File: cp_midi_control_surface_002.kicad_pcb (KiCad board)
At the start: 2 copper layers, 185 parts, among them J1 Conn_01x08_Male, J10 Conn_01x08_Female, J11 Conn_01x08_Female, J12 Conn_01x08_Female, J13 Conn_01x08_Female, J14 Conn_01x08_Female, J15 Conn_01x08_Female, J16 Conn_01x08_Female, J17 Conn_01x08_Female, J18 Conn_01x01_Male, J19 Conn_01x01_Male, J2 Conn_01x08_Male, J20 Conn_01x01_Male, J21 Conn_01x01_Male, J22 Conn_01x01_Male, J23 Conn_01x01_Male, J3 Conn_01x08_Male, J4 Conn_01x01_Male, J5 Conn_01x01_Male, J6 Conn_01x01_Male, J7 Conn_01x01_Male, J8 Conn_01x08_Male, J9 Conn_01x08_Male, P1 Digital, P10 CONN_01X01, P11 CONN_01X01, P12 CONN_01X01, P13 CONN_01X01, P2 Power, P3 Analogue, P4 Analogue, P5 PWM, P6 PWM, P7 Communication, P8 CONN_01X01, P9 CONN_01X01, SW1 SW_SPST_4_PIN, SW10 SW_SPST_4_PIN, SW11 SW_SPST_4_PIN, SW12 SW_SPST_4_PIN, SW13 SW_SPST_4_PIN, SW14 SW_SPST_4_PIN, SW15 SW_SPST_4_PIN, SW16 SW_SPST_4_PIN, SW17 SW_SPST_4_PIN, SW18 SW_SPST_4_PIN, SW19 SW_SPST_4_PIN, SW2 SW_SPST_4_PIN, SW20 SW_SPST_4_PIN, SW21 SW_SPST_4_PIN, SW22 SW_SPST_4_PIN, SW23 SW_SPST_4_PIN, SW24 SW_SPST_4_PIN, SW25 SW_SPST_4_PIN, SW26 SW_SPST_4_PIN, SW27 SW_SPST_4_PIN, SW28 SW_SPST_4_PIN, SW29 SW_SPST_4_PIN, SW3 SW_SPST_4_PIN, SW30 SW_SPST_4_PIN, SW31 SW_SPST_4_PIN, SW32 SW_SPST_4_PIN, SW33 SW_SPST_4_PIN, SW34 SW_SPST_4_PIN, SW35 SW_SPST_4_PIN, SW36 SW_SPST_4_PIN, SW37 SW_SPST_4_PIN, SW38 SW_SPST_4_PIN, SW39 SW_SPST_4_PIN, SW4 SW_SPST_4_PIN, SW40 SW_SPST_4_PIN, SW41 SW_SPST_4_PIN, SW42 SW_SPST_4_PIN, SW43 SW_SPST_4_PIN, SW44 SW_SPST_4_PIN, SW45 SW_SPST_4_PIN, SW46 SW_SPST_4_PIN, SW47 SW_SPST_4_PIN, SW48 SW_SPST_4_PIN, SW49 SW_SPST_4_PIN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

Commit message: First of changes due to different software
Moving and analogue inputs, correcting for placement of multiplexer pads.
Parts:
- removed P4: Analogue, Connector_PinHeader_2.54mm:PinHeader_1x08_P2.54mm_Vertical
- P7: footprint Connector_PinHeader_2.54mm:PinHeader_1x08_P2.54mm_Vertical -> Connector_PinHeader_2.54mm:PinHeader_1x04_P2.54mm_Vertical
- moved H1 199.0 mm to (764.4, 381.0)
- moved H10 199.0 mm to (761.1, 395.1)
- moved H11 199.0 mm to (759.4, 401.3)
- moved H13 199.0 mm to (765.8, 395.1)
- moved H14 199.0 mm to (754.7, 401.3)
- moved H2 199.0 mm to (759.7, 385.7)
- moved H21 199.0 mm to (761.1, 390.4)
- moved H22 199.0 mm to (746.9, 391.9)
- moved H24 199.0 mm to (746.9, 396.6)
- moved H3 199.0 mm to (759.7, 381.0)
- moved H5 199.0 mm to (764.4, 385.7)
- moved H7 199.0 mm to (773.9, 381.0)
- moved H8 199.0 mm to (773.9, 385.7)
- moved H9 199.0 mm to (765.8, 390.4)
- moved J10 199.0 mm to (737.4, 400.7)
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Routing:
- net /A2: track 342.2 -> 0.00 mm
- net /A3: track 316.7 -> 0.00 mm
- net /A4: track 291.1 -> 0.00 mm
- net /A5: track 265.6 -> 0.00 mm
- net /A6: track 240.1 -> 0.00 mm
- net /A7: track 214.5 -> 0.00 mm
- net /A1: track 367.8 -> 167.6 mm
- net /A8: track 186.5 -> 0.00 mm
- net +5V: track 1386.4 -> 1350.2 mm

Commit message: Sub boards completed
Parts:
- added J24: Conn_01x04_Male, Connector_PinHeader_2.54mm:PinHeader_1x04_P2.54mm_Vertical, F.Cu at (180.0, 239.2)
- added U6: CD74HC4067M, Package_SO:SOIC-24W_7.5x15.4mm_P1.27mm, B.Cu at (421.4, 273.6)
- H1, H10, H11, H12, H13, H14, H15, H16, H17, H18, H19, H2, H20, H21, H22, H23, H24, H25, H26, H3, H4, H5, H6, H7, H8, H9: footprint cunabulapress-footprints:Mounting_Hole_3.2mm_M3 -> cunabulapress-footprints:Mounting_Hole_M3_with_Target
- J11: moved to B.Cu
- J3: value Conn_01x08_Male -> Conn_01x04_Male; footprint Connector_PinHeader_2.54mm:PinHeader_1x08_P2.54mm_Vertical -> Connector_PinHeader_2.54mm:PinHeader_1x04_P2.54mm_Vertical
- moved H1 726.8 mm to (74.2, 153.0)
- moved H3 709.4 mm to (74.2, 198.0)
- moved H2 651.9 mm to (150.8, 153.0)
- moved J11 649.0 mm to (116.7, 259.5)
- moved H4 645.7 mm to (150.8, 198.2)
- moved H5 643.7 mm to (164.2, 153.0)
- moved H7 636.5 mm to (164.2, 198.0)
- moved H6 577.4 mm to (240.8, 153.0)
- moved H8 565.2 mm to (240.8, 198.0)
- moved H9 557.9 mm to (264.0, 146.7)
- moved H11 534.5 mm to (264.0, 200.7)
- moved J6 518.9 mm to (70.2, 249.2)
- moved J4 510.6 mm to (70.2, 236.8)
- moved J16 476.9 mm to (206.7, 199.3)
- moved H10 474.3 mm to (357.0, 146.7)
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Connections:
- net /A10 renamed /Lower Pots/LOWER_POTS
- net /A8 renamed Net-(RV8-Pad2)
- J10 pad 1: Mult_1 -> S0
- J10 pad 2: Mult_2 -> S1
- J10 pad 3: Mult_3 -> S3
- J10 pad 4: Mult_4 -> S2
- J10 pad 5: /A9 -> /A0
- J11 pad 1: Mult_1 -> S0
- J11 pad 2: Mult_2 -> S1
- J11 pad 3: Mult_3 -> S3
- J11 pad 4: Mult_4 -> S2
- J11 pad 5: /52 -> /A1
- J12 pad 1: Mult_1 -> S0
- J12 pad 2: Mult_2 -> S1
- J12 pad 3: Mult_3 -> S3
- J12 pad 4: Mult_4 -> S2
- J12 pad 5: /50 -> /A2
- J13 pad 1: Mult_1 -> S0
- J13 pad 2: Mult_2 -> S1
- J13 pad 3: Mult_3 -> S3
- J13 pad 4: Mult_4 -> S2
- J13 pad 5: /48 -> /A3
- J3 pad 1: /46 -> Net-(J3-Pad1)
- J3 pad 2: /44 -> Net-(J3-Pad2)
- J3 pad 3: /42 -> Net-(J3-Pad3)
- J3 pad 4: /40 -> Net-(J3-Pad4)
- P1 pad 10: /36 -> /37
- P1 pad 11: /34 -> /35
- P1 pad 12: /32 -> /33
- P1 pad 14: /28 -> S2
- P1 pad 15: /26 -> S3
- P1 pad 16: Net-(P1-Pad16) -> S1
- P1 pad 17: Net-(P1-Pad17) -> S0
- P1 pad 2: /52 -> /53
- P1 pad 3: /50 -> /51
- P1 pad 4: /48 -> /49
- P1 pad 5: /46 -> /47
- P1 pad 6: /44 -> /45
- P1 pad 7: /42 -> /43
- P1 pad 8: /40 -> /41
- P1 pad 9: /38 -> /39
- P3 pad 7: /A6 -> Net-(P3-Pad7)
- P3 pad 8: /A7 -> Net-(P3-Pad8)
- RV1 pad 2: /A1 -> Net-(RV1-Pad2)
- RV2 pad 2: /A2 -> Net-(RV2-Pad2)
- RV3 pad 2: /A3 -> Net-(RV3-Pad2)
- RV4 pad 2: /A4 -> Net-(RV4-Pad2)
- RV5 pad 2: /A5 -> Net-(RV5-Pad2)
- RV6 pad 2: /A6 -> Net-(RV6-Pad2)
- RV7 pad 2: /A7 -> Net-(RV7-Pad2)
- RVM1 pad 2: /A0 -> Net-(RVM1-Pad2)
- SW1 pad 3: GND -> Net-(SW1-Pad3)
- SW1 pad 4: Net-(SW1-Pad4) -> GND
- SW33 pad 1: Net-(SW33-Pad1) -> Net-(J3-Pad1)
- SW33 pad 2: /46 -> Net-(SW33-Pad2)
- SW34 pad 1: Net-(SW34-Pad1) -> Net-(J3-Pad2)
- SW34 pad 2: /44 -> Net-(SW34-Pad2)
- SW35 pad 1: Net-(SW35-Pad1) -> Net-(J3-Pad3)
- SW35 pad 2: /42 -> Net-(SW35-Pad2)
- SW36 pad 1: Net-(SW36-Pad1) -> Net-(J3-Pad4)
- SW36 pad 2: /40 -> Net-(SW36-Pad2)
- SW37 pad 1: /38 -> Net-(J24-Pad1)
- SW38 pad 1: /36 -> Net-(J24-Pad2)
- SW39 pad 1: /34 -> Net-(J24-Pad3)
- SW40 pad 1: /32 -> Net-(J24-Pad4)
- SW_F1 pad 12: /A0 -> Net-(RVM1-Pad2)
- SW_F1 pad 14: /A7 -> Net-(RV7-Pad2)
- SW_F1 pad 15: /A6 -> Net-(RV6-Pad2)
- SW_F1 pad 16: /A5 -> Net-(RV5-Pad2)
- SW_F1 pad 17: /A4 -> Net-(RV4-Pad2)
- SW_F1 pad 18: /A3 -> Net-(RV3-Pad2)
- SW_F1 pad 19: /A2 -> Net-(RV2-Pad2)
- SW_F1 pad 20: /A1 -> Net-(RV1-Pad2)
- SW_M1 pad A: /28 -> /37
- SW_M1 pad B: /26 -> /35
- U1 pad 13: Net-(J15-Pad4) -> Net-(J15-Pad3)
- U1 pad 14: Net-(J15-Pad3) -> Net-(J15-Pad4)
- U2 pad 13: Net-(J16-Pad4) -> Net-(J16-Pad3)
- U2 pad 14: Net-(J16-Pad3) -> Net-(J16-Pad4)
- U3 pad 13: Net-(J14-Pad4) -> Net-(J14-Pad3)
- U3 pad 14: Net-(J14-Pad3) -> Net-(J14-Pad4)
- U4 pad 13: Net-(J17-Pad4) -> Net-(J17-Pad3)
- U4 pad 14: Net-(J17-Pad3) -> Net-(J17-Pad4)
- U5 pad 10: Mult_1 -> S0
- U5 pad 11: Mult_2 -> S1
- U5 pad 13: Mult_4 -> S3
- U5 pad 14: Mult_3 -> S2
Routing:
- net +5V: track 1350.2 -> 1074.5 mm, vias 0 -> 3
- net /A1: track 167.6 -> 0.00 mm
- net Net-(J14-Pad5): track 185.2 -> 45.9 mm, vias 0 -> 1
- net Net-(J17-Pad5): track 138.8 -> 41.4 mm, vias 0 -> 1
- net Net-(J15-Pad5): track 135.6 -> 41.3 mm, vias 0 -> 1
- net Net-(J16-Pad5): track 134.7 -> 41.3 mm, vias 0 -> 1
- net Net-(J14-Pad1): track 85.2 -> 26.8 mm
- net Net-(J14-Pad2): track 80.2 -> 22.3 mm
- net Net-(J24-Pad2): track 0.00 -> 57.3 mm
- net Net-(J3-Pad3): track 0.00 -> 57.3 mm
- net Net-(J14-Pad3): track 79.5 -> 23.9 mm
- net Net-(J14-Pad4): track 74.2 -> 23.7 mm
- net Net-(J3-Pad2): track 0.00 -> 33.3 mm
- net Net-(J24-Pad3): track 0.00 -> 33.3 mm
- net Net-(J15-Pad1): track 54.7 -> 22.2 mm
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
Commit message: Tidy schematic / renumber components / complete daughter boards
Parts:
- removed the J5 at (244.8, 236.8)
- removed the J6 at (70.2, 249.2)
- removed the J8 at (654.5, 169.8)
- removed the P1 at (374.5, 266.8)
- removed the P5 at (452.3, 310.0)
- removed the U1 at (112.5, 175.5)
- added J13: ~, Connector_PinHeader_2.54mm:PinHeader_1x01_P2.54mm_Vertical, B.Cu at (262.8, 89.2)
- added J14: ~, Connector_PinSocket_2.54mm:PinSocket_1x01_P2.54mm_Vertical, F.Cu at (70.2, 236.8)
- added J15: ~, Connector_PinHeader_2.54mm:PinHeader_1x01_P2.54mm_Vertical, B.Cu at (437.2, 89.2)
- added J25: ~, Connector_PinHeader_2.54mm:PinHeader_1x08_P2.54mm_Vertical, B.Cu at (379.9, 112.8)
- added J26: ~, Connector_PinSocket_2.54mm:PinSocket_1x08_P2.54mm_Vertical, F.Cu at (270.0, 236.0)
- added J27: ~, Connector_PinHeader_2.54mm:PinHeader_1x08_P2.54mm_Vertical, B.Cu at (443.1, 112.8)
- added J28: ~, Connector_PinSocket_2.54mm:PinSocket_1x08_P2.54mm_Vertical, F.Cu at (333.2, 236.0)
- added P2: Analogue, Connector_PinHeader_2.54mm:PinHeader_1x08_P2.54mm_Vertical, B.Cu at (420.3, 262.7)
- added P6: PWM, Connector_PinHeader_2.54mm:PinHeader_1x10_P2.54mm_Vertical, B.Cu at (452.3, 311.0)
- added REF**: Clearance_Hole_M3, cunabulapress-footprints:Clearance_Hole_M3, F.Cu at (350.0, 95.5)
- added U6: CD74HC4067M, Package_SO:SOIC-24W_7.5x15.4mm_P1.27mm, B.Cu at (310.0, 281.5)
- D1, D10, D11, D12, D13, D14, D15, D16, D2, D3, D4, D5, D6, D7, D8, D9: value ~ -> LED
- H1, H10, H11, H12, H13, H14, H15, H16, H17, H18, H19, H2, H20, H21, H22, H23, H24, H25, H26, H3, H4, H5, H6, H7, H8, H9: value MountingHole -> ~
- J1, J2: value Conn_01x08_Male -> ~; footprint Connector_PinHeader_2.54mm:PinHeader_1x08_P2.54mm_Vertical -> cunabulapress-footprints:Connector_TE_Connectivity_Micro-MaTch_8_Position_Female; moved to B.Cu
- J10, J12: value Conn_01x08_Female -> ~; footprint cunabulapress-footprints:Connector_TE_Connectivity_Micro-MaTch_8_Position_Female -> Connector_PinSocket_2.54mm:PinSocket_1x04_P2.54mm_Vertical; moved to F.Cu
- J11: value Conn_01x08_Female -> ~; footprint cunabulapress-footprints:Connector_TE_Connectivity_Micro-MaTch_8_Position_Female -> Connector_PinHeader_2.54mm:PinHeader_1x04_P2.54mm_Vertical
- J16: value Conn_01x08_Female -> ~; footprint cunabulapress-footprints:Connector_TE_Connectivity_Micro-MaTch_8_Position_Female -> Connector_PinSocket_2.54mm:PinSocket_1x01_P2.54mm_Vertical; moved to F.Cu
- J17: value Conn_01x08_Female -> ~; footprint cunabulapress-footprints:Connector_TE_Connectivity_Micro-MaTch_8_Position_Female -> Connector_PinHeader_2.54mm:PinHeader_1x01_P2.54mm_Vertical
- J18, J20: value Conn_01x01_Male -> ~; footprint cunabulapress-footprints:Arduino_1pin_EDIT -> Connector_PinSocket_2.54mm:PinSocket_1x01_P2.54mm_Vertical
- J19: value Conn_01x01_Male -> ~; footprint cunabulapress-footprints:Arduino_1pin_EDIT -> Connector_PinHeader_2.54mm:PinHeader_1x01_P2.54mm_Vertical; moved to B.Cu
- J21, J23: value Conn_01x01_Male -> ~; footprint cunabulapress-footprints:Arduino_1pin_EDIT -> Connector_PinHeader_2.54mm:PinHeader_1x08_P2.54mm_Vertical; moved to B.Cu
- J22: value Conn_01x01_Male -> ~; footprint cunabulapress-footprints:Arduino_1pin_EDIT -> Connector_PinSocket_2.54mm:PinSocket_1x08_P2.54mm_Vertical
- J24: value Conn_01x04_Male -> ~; footprint Connector_PinHeader_2.54mm:PinHeader_1x04_P2.54mm_Vertical -> Connector_PinSocket_2.54mm:PinSocket_1x08_P2.54mm_Vertical
- J3: value Conn_01x04_Male -> ~; footprint Connector_PinHeader_2.54mm:PinHeader_1x04_P2.54mm_Vertical -> cunabulapress-footprints:Connector_TE_Connectivity_Micro-MaTch_8_Position_Female; moved to B.Cu
- J4, J7: value Conn_01x01_Male -> ~; footprint Connector_PinHeader_2.54mm:PinHeader_1x01_P2.54mm_Vertical -> cunabulapress-footprints:Connector_TE_Connectivity_Micro-MaTch_8_Position_Female; moved to B.Cu
- J5: renamed from J13; value Conn_01x08_Female -> ~
- J6: renamed from J15; value Conn_01x08_Female -> ~
- J8: renamed from J14; value Conn_01x08_Female -> ~
- J9: value Conn_01x08_Male -> ~; footprint Connector_PinHeader_2.54mm:PinHeader_1x08_P2.54mm_Vertical -> Connector_PinHeader_2.54mm:PinHeader_1x04_P2.54mm_Vertical; moved to B.Cu
- P10, P11, P12, P13, P8, P9: value CONN_01X01 -> Guide
- P3: value Analogue -> Digital; footprint Connector_PinHeader_2.54mm:PinHeader_1x08_P2.54mm_Vertical -> Connector_PinHeader_2.54mm:PinHeader_1x18_P2.54mm_Vertical
- RN1: value R_Network09 -> 2.2K (Bussed)
- RN2, RN3: value R_Network08 -> 680Ω (Bussed)
- RV1, RV2, RV3, RV4, RV5, RV6, RV7, RV8, RVM1: value 10k -> PTA4543
- RVCF1: value R_POT -> PTA4543
- SW1, SW10, SW11, SW12, SW13, SW14, SW15, SW16, SW17, SW18, SW19, SW2, SW20, SW21, SW22, SW23, SW24, SW25, SW26, SW27, SW28, SW29, SW3, SW30, SW31, SW32, SW33, SW34, SW35, SW36, SW37, SW38, SW39, SW4, SW40, SW41, SW42, SW43, SW44, SW45, SW46, SW47, SW48, SW49, SW5, SW50, SW51, SW52, SW53, SW54, SW55, SW56, SW6, SW7, SW8, SW9: value SW_SPST_4_PIN -> B3F-5050
- SW_M1: value Mode Switch -> EC12E
- moved SW_F1 671.7 mm to (-67.8, 227.2), turned to 90 degrees
- moved RN1 602.1 mm to (-24.2, 219.8)
- moved J1 545.9 mm to (116.7, 199.3)
- moved J2 541.6 mm to (116.7, 259.5)
- moved J18 455.7 mm to (70.2, 249.2)
- moved H23 427.7 mm to (157.5, 326.2)
- moved H18 416.2 mm to (157.2, 243.0)
- moved RN2 364.9 mm to (267.4, 232.2)
- moved J9 339.8 mm to (327.5, 91.8), turned to 180 degrees
- moved H19 325.2 mm to (252.0, 243.0)
- moved U1 324.1 mm to (112.5, 175.5), turned to 180 degrees
- moved H24 319.9 mm to (251.3, 326.0)
- moved J11 305.9 mm to (372.5, 91.8), turned to 180 degrees
- moved RN3 302.2 mm to (330.7, 232.2)
- moved J20 295.1 mm to (244.8, 249.2)
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- renumbered P2 to P1, P7 to P4, P6 to P5, U6 to U1, U3 to U2, U5 to U3, U2 to U5
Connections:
- D1 pad 2: /17 -> Net-(D1-Pad2)
- D10 pad 2: /7 -> Net-(D10-Pad2)
- D11 pad 2: /8 -> Net-(D11-Pad2)
- D12 pad 2: /9 -> Net-(D12-Pad2)
- D13 pad 2: /10 -> Net-(D13-Pad2)
- D14 pad 2: /11 -> Net-(D14-Pad2)
- D15 pad 2: /12 -> Net-(D15-Pad2)
- D16 pad 2: /13 -> Net-(D16-Pad2)
- D2 pad 2: /16 -> Net-(D2-Pad2)
- D3 pad 2: /15 -> Net-(D3-Pad2)
- D4 pad 2: /14 -> Net-(D4-Pad2)
- D5 pad 2: /2 -> Net-(D5-Pad2)
- D6 pad 2: /3 -> Net-(D6-Pad2)
- D7 pad 2: /4 -> Net-(D7-Pad2)
- D8 pad 2: /5 -> Net-(D8-Pad2)
- D9 pad 2: /6 -> Net-(D9-Pad2)
- J1 pad 1: /17 -> Net-(J1-Pad1)
- J1 pad 2: /16 -> Net-(J1-Pad2)
- J1 pad 3: /15 -> Net-(J1-Pad3)
- J1 pad 4: /14 -> Net-(J1-Pad4)
- J1 pad 5: /2 -> Net-(J1-Pad5)
- J1 pad 6: /3 -> +5V
- J1 pad 7: /4 -> GND
- J1 pad 8: /5 -> Net-(J1-Pad8)
- J10 pad 1: S0 -> /53
- J10 pad 2: S1 -> /51
- J10 pad 3: S3 -> /49
- J10 pad 4: S2 -> /47
- J11 pad 1: S0 -> Net-(J11-Pad1)
- J11 pad 2: S1 -> Net-(J11-Pad2)
- J11 pad 3: S3 -> Net-(J11-Pad3)
- J11 pad 4: S2 -> Net-(J11-Pad4)
- J12 pad 1: S0 -> /45
- J12 pad 2: S1 -> /43
- J12 pad 3: S3 -> /41
- J12 pad 4: S2 -> /39
- J16 pad 1: Net-(J16-Pad1) -> GND
- J17 pad 1: Net-(J17-Pad1) -> GND
- J2 pad 1: /6 -> S0
- J2 pad 2: /7 -> S1
- J2 pad 3: /8 -> S3
- J2 pad 4: /9 -> S2
- J2 pad 5: /10 -> /A0
- J2 pad 6: /11 -> +5V
- J2 pad 7: /12 -> GND
- J2 pad 8: /13 -> Net-(J2-Pad8)
- J24 pad 1: Net-(J24-Pad1) -> /6
- J24 pad 2: Net-(J24-Pad2) -> /7
- J24 pad 3: Net-(J24-Pad3) -> /8
- J24 pad 4: Net-(J24-Pad4) -> /9
- J4 pad 1: GND -> S0
- J5 pad 1: S0 -> Net-(J5-Pad1)
- J5 pad 2: S1 -> Net-(J5-Pad2)
- J5 pad 3: S3 -> Net-(J5-Pad3)
- J5 pad 4: S2 -> Net-(J5-Pad4)
- J5 pad 5: /A3 -> Net-(J5-Pad5)
- J6 pad 1: Net-(J15-Pad1) -> S0
- J6 pad 2: Net-(J15-Pad2) -> S1
- J6 pad 3: Net-(J15-Pad3) -> S3
- J6 pad 4: Net-(J15-Pad4) -> S2
- J6 pad 5: Net-(J15-Pad5) -> /A2
- J7 pad 1: GND -> Net-(J7-Pad1)
- J8 pad 1: Net-(J14-Pad1) -> S0
- J8 pad 2: Net-(J14-Pad2) -> S1
- J8 pad 3: Net-(J14-Pad3) -> S3
- J8 pad 4: Net-(J14-Pad4) -> S2
- J8 pad 5: Net-(J14-Pad5) -> /A3
- J9 pad 1: Net-(D9-Pad1) -> Net-(J9-Pad1)
- J9 pad 2: Net-(D10-Pad1) -> Net-(J9-Pad2)
- J9 pad 3: Net-(D11-Pad1) -> Net-(J9-Pad3)
- J9 pad 4: Net-(D12-Pad1) -> Net-(J9-Pad4)
- P3 pad 1: /A0 -> GND
- P3 pad 2: /A1 -> /53
- P3 pad 3: /A2 -> /51
- P3 pad 4: /A3 -> /49
- P3 pad 5: /A4 -> /47
- P3 pad 6: /A5 -> /45
- P3 pad 7: Net-(P3-Pad7) -> /43
- P3 pad 8: Net-(P3-Pad8) -> /41
- RN2 pad 2: Net-(D1-Pad1) -> Net-(J26-Pad1)
- RN2 pad 3: Net-(D2-Pad1) -> Net-(J26-Pad2)
- RN2 pad 4: Net-(D3-Pad1) -> Net-(J26-Pad3)
- RN2 pad 5: Net-(D4-Pad1) -> Net-(J26-Pad4)
- RN2 pad 6: Net-(D5-Pad1) -> Net-(J26-Pad5)
- RN2 pad 7: Net-(D6-Pad1) -> Net-(J26-Pad6)
- RN2 pad 8: Net-(D7-Pad1) -> Net-(J26-Pad7)
- RN2 pad 9: Net-(D8-Pad1) -> Net-(J26-Pad8)
- RN3 pad 2: Net-(D9-Pad1) -> Net-(J28-Pad1)
- RN3 pad 3: Net-(D10-Pad1) -> Net-(J28-Pad2)
- RN3 pad 4: Net-(D11-Pad1) -> Net-(J28-Pad3)
- RN3 pad 5: Net-(D12-Pad1) -> Net-(J28-Pad4)
- RN3 pad 6: Net-(D13-Pad1) -> Net-(J28-Pad5)
- RN3 pad 7: Net-(D14-Pad1) -> Net-(J28-Pad6)
- RN3 pad 8: Net-(D15-Pad1) -> Net-(J28-Pad7)
- RN3 pad 9: Net-(D16-Pad1) -> Net-(J28-Pad8)
- SW33 pad 1: Net-(J3-Pad1) -> Net-(J9-Pad1)
- SW34 pad 1: Net-(J3-Pad2) -> Net-(J9-Pad2)
- SW35 pad 1: Net-(J3-Pad3) -> Net-(J9-Pad3)
- SW36 pad 1: Net-(J3-Pad4) -> Net-(J9-Pad4)
- SW37 pad 1: Net-(J24-Pad1) -> Net-(J11-Pad1)
- SW38 pad 1: Net-(J24-Pad2) -> Net-(J11-Pad2)
- SW39 pad 1: Net-(J24-Pad3) -> Net-(J11-Pad3)
- SW40 pad 1: Net-(J24-Pad4) -> Net-(J11-Pad4)
- SW_F1 pad 1: Net-(RN1-Pad10) -> Net-(RV1-Pad2)
- SW_F1 pad 12: Net-(RVM1-Pad2) -> Net-(RN1-Pad2)
- SW_F1 pad 13: Net-(RV8-Pad2) -> Net-(RN1-Pad3)
- SW_F1 pad 14: Net-(RV7-Pad2) -> Net-(RN1-Pad4)
- SW_F1 pad 15: Net-(RV6-Pad2) -> Net-(RN1-Pad5)
- SW_F1 pad 16: Net-(RV5-Pad2) -> Net-(RN1-Pad6)
- SW_F1 pad 17: Net-(RV4-Pad2) -> Net-(RN1-Pad7)
- SW_F1 pad 18: Net-(RV3-Pad2) -> Net-(RN1-Pad8)
- SW_F1 pad 19: Net-(RV2-Pad2) -> Net-(RN1-Pad9)
- SW_F1 pad 2: Net-(RN1-Pad9) -> Net-(RV2-Pad2)
- SW_F1 pad 20: Net-(RV1-Pad2) -> Net-(RN1-Pad10)
- SW_F1 pad 3: Net-(RN1-Pad8) -> Net-(RV3-Pad2)
- SW_F1 pad 4: Net-(RN1-Pad7) -> Net-(RV4-Pad2)
- SW_F1 pad 5: Net-(RN1-Pad6) -> Net-(RV5-Pad2)
- SW_F1 pad 6: Net-(RN1-Pad5) -> Net-(RV6-Pad2)
- SW_F1 pad 7: Net-(RN1-Pad4) -> Net-(RV7-Pad2)
- SW_F1 pad 8: Net-(RN1-Pad3) -> Net-(RV8-Pad2)
- SW_F1 pad 9: Net-(RN1-Pad2) -> Net-(RVM1-Pad2)
- U1 pad 1: /A5 -> Net-(J1-Pad5)
- U1 pad 10: S0 -> Net-(J1-Pad1)
- U1 pad 11: S1 -> Net-(J1-Pad2)
- U1 pad 13: S3 -> Net-(J1-Pad3)
- U1 pad 14: S2 -> Net-(J1-Pad4)
- U1 pad 16: Net-(U6-Pad16) -> Net-(SW16-Pad1)
- U1 pad 17: Net-(U6-Pad17) -> Net-(SW15-Pad1)
- U1 pad 18: Net-(U6-Pad18) -> Net-(SW14-Pad1)
- U1 pad 19: Net-(U6-Pad19) -> Net-(SW13-Pad1)
- U1 pad 2: Net-(RV8-Pad2) -> Net-(SW8-Pad1)
- U1 pad 20: Net-(U6-Pad20) -> Net-(SW12-Pad2)
- U1 pad 21: Net-(U6-Pad21) -> Net-(SW11-Pad2)
- U1 pad 22: Net-(U6-Pad22) -> Net-(SW10-Pad2)
- U1 pad 23: Net-(RVM1-Pad2) -> Net-(SW9-Pad2)
- U1 pad 3: Net-(RV7-Pad2) -> Net-(SW7-Pad1)
- U1 pad 4: Net-(RV6-Pad2) -> Net-(SW6-Pad1)
- U1 pad 5: Net-(RV5-Pad2) -> Net-(SW5-Pad1)
- U1 pad 6: Net-(RV4-Pad2) -> Net-(SW4-Pad2)
- U1 pad 7: Net-(RV3-Pad2) -> Net-(SW3-Pad2)
- U1 pad 8: Net-(RV2-Pad2) -> Net-(SW2-Pad2)
- U1 pad 9: Net-(RV1-Pad2) -> Net-(SW1-Pad2)
- U2 pad 1: Net-(J14-Pad5) -> Net-(J3-Pad5)
- U2 pad 10: Net-(J14-Pad1) -> Net-(J3-Pad1)
- U2 pad 11: Net-(J14-Pad2) -> Net-(J3-Pad2)
- U2 pad 13: Net-(J14-Pad3) -> Net-(J3-Pad3)
- U2 pad 14: Net-(J14-Pad4) -> Net-(J3-Pad4)
- U2 pad 16: Net-(PT_16-Pad2) -> Net-(SW32-Pad1)
- U2 pad 17: Net-(PT_15-Pad2) -> Net-(SW31-Pad1)
- U2 pad 18: Net-(PT_14-Pad2) -> Net-(SW30-Pad1)
- U2 pad 19: Net-(PT_13-Pad2) -> Net-(SW29-Pad1)
- U2 pad 2: Net-(PT_8-Pad2) -> Net-(SW24-Pad1)
- U2 pad 20: Net-(PT_12-Pad2) -> Net-(SW28-Pad2)
- U2 pad 21: Net-(PT_11-Pad2) -> Net-(SW27-Pad2)
- U2 pad 22: Net-(PT_10-Pad2) -> Net-(SW26-Pad2)
- U2 pad 23: Net-(PT_9-Pad2) -> Net-(SW25-Pad2)
- U2 pad 3: Net-(PT_7-Pad2) -> Net-(SW23-Pad1)
- U2 pad 4: Net-(PT_6-Pad2) -> Net-(SW22-Pad1)
- U2 pad 5: Net-(PT_5-Pad2) -> Net-(SW21-Pad1)
- U2 pad 6: Net-(PT_4-Pad2) -> Net-(SW20-Pad2)
- U2 pad 7: Net-(PT_3-Pad2) -> Net-(SW19-Pad2)
- U2 pad 8: Net-(PT_2-Pad2) -> Net-(SW18-Pad2)
- U2 pad 9: Net-(PT_1-Pad2) -> Net-(SW17-Pad2)
- U3 pad 1: /Lower Pots/LOWER_POTS -> Net-(J5-Pad5)
- U3 pad 10: S0 -> Net-(J5-Pad1)
- U3 pad 11: S1 -> Net-(J5-Pad2)
- U3 pad 13: S3 -> Net-(J5-Pad3)
- U3 pad 14: S2 -> Net-(J5-Pad4)
- U3 pad 16: Net-(RVCF1-Pad2) -> Net-(PT_16-Pad2)
- U3 pad 17: Net-(PT_31-Pad2) -> Net-(PT_15-Pad2)
- U3 pad 18: Net-(PT_30-Pad2) -> Net-(PT_14-Pad2)
- U3 pad 19: Net-(PT_29-Pad2) -> Net-(PT_13-Pad2)
- U3 pad 2: Net-(PT_24-Pad2) -> Net-(PT_8-Pad2)
- U3 pad 20: Net-(PT_28-Pad2) -> Net-(PT_12-Pad2)
- U3 pad 21: Net-(PT_27-Pad2) -> Net-(PT_11-Pad2)
- U3 pad 22: Net-(PT_26-Pad2) -> Net-(PT_10-Pad2)
- U3 pad 23: Net-(PT_25-Pad2) -> Net-(PT_9-Pad2)
- U3 pad 3: Net-(PT_23-Pad2) -> Net-(PT_7-Pad2)
- U3 pad 4: Net-(PT_22-Pad2) -> Net-(PT_6-Pad2)
- U3 pad 5: Net-(PT_21-Pad2) -> Net-(PT_5-Pad2)
- U3 pad 6: Net-(PT_20-Pad2) -> Net-(PT_4-Pad2)
- U3 pad 7: Net-(PT_19-Pad2) -> Net-(PT_3-Pad2)
- U3 pad 8: Net-(PT_18-Pad2) -> Net-(PT_2-Pad2)
- U3 pad 9: Net-(PT_17-Pad2) -> Net-(PT_1-Pad2)
- U4 pad 1: Net-(J17-Pad5) -> Net-(J7-Pad5)
- U4 pad 10: Net-(J17-Pad1) -> Net-(J7-Pad1)
- U4 pad 11: Net-(J17-Pad2) -> Net-(J7-Pad2)
- U4 pad 13: Net-(J17-Pad3) -> Net-(J7-Pad3)
- U4 pad 14: Net-(J17-Pad4) -> Net-(J7-Pad4)
- U5 pad 1: Net-(J16-Pad5) -> /A5
- U5 pad 10: Net-(J16-Pad1) -> S0
- U5 pad 11: Net-(J16-Pad2) -> S1
- U5 pad 13: Net-(J16-Pad3) -> S3
- U5 pad 14: Net-(J16-Pad4) -> S2
- U5 pad 16: Net-(SW32-Pad1) -> Net-(U5-Pad16)
- U5 pad 17: Net-(SW31-Pad1) -> Net-(U5-Pad17)
- U5 pad 18: Net-(SW30-Pad1) -> Net-(U5-Pad18)
- U5 pad 19: Net-(SW29-Pad1) -> Net-(U5-Pad19)
- U5 pad 2: Net-(SW24-Pad1) -> Net-(RV8-Pad2)
- U5 pad 20: Net-(SW28-Pad2) -> Net-(U5-Pad20)
- U5 pad 21: Net-(SW27-Pad2) -> Net-(U5-Pad21)
- U5 pad 22: Net-(SW26-Pad2) -> Net-(U5-Pad22)
- U5 pad 23: Net-(SW25-Pad2) -> Net-(RVM1-Pad2)
- U5 pad 3: Net-(SW23-Pad1) -> Net-(RV7-Pad2)
- U5 pad 4: Net-(SW22-Pad1) -> Net-(RV6-Pad2)
- U5 pad 5: Net-(SW21-Pad1) -> Net-(RV5-Pad2)
- U5 pad 6: Net-(SW20-Pad2) -> Net-(RV4-Pad2)
- U5 pad 7: Net-(SW19-Pad2) -> Net-(RV3-Pad2)
- U5 pad 8: Net-(SW18-Pad2) -> Net-(RV2-Pad2)
- U5 pad 9: Net-(SW17-Pad2) -> Net-(RV1-Pad2)
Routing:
- net S3: track 0.00 -> 218.3 mm
- net S1: track 0.00 -> 218.3 mm
- net S0: track 0.00 -> 217.2 mm
- net S2: track 0.00 -> 217.0 mm
- net Net-(J11-Pad4): track 0.00 -> 65.1 mm
- net Net-(J9-Pad1): track 0.00 -> 65.1 mm
- net Net-(J24-Pad2): track 57.3 -> 0.00 mm
- net Net-(J5-Pad5): track 0.00 -> 45.9 mm, vias 0 -> 1
- net Net-(J14-Pad5): track 45.9 -> 0.00 mm, vias 1 -> 0
- net Net-(J9-Pad2): track 0.00 -> 41.8 mm
- net Net-(J11-Pad3): track 0.00 -> 41.7 mm
- net Net-(J7-Pad5): track 0.00 -> 41.4 mm, vias 0 -> 1
- net Net-(J17-Pad5): track 41.4 -> 0.00 mm, vias 1 -> 0
- net Net-(J15-Pad5): track 41.3 -> 0.00 mm, vias 1 -> 0
- net Net-(J1-Pad5): track 0.00 -> 41.3 mm, vias 0 -> 1
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- added copper zone on F.Cu, net (none)

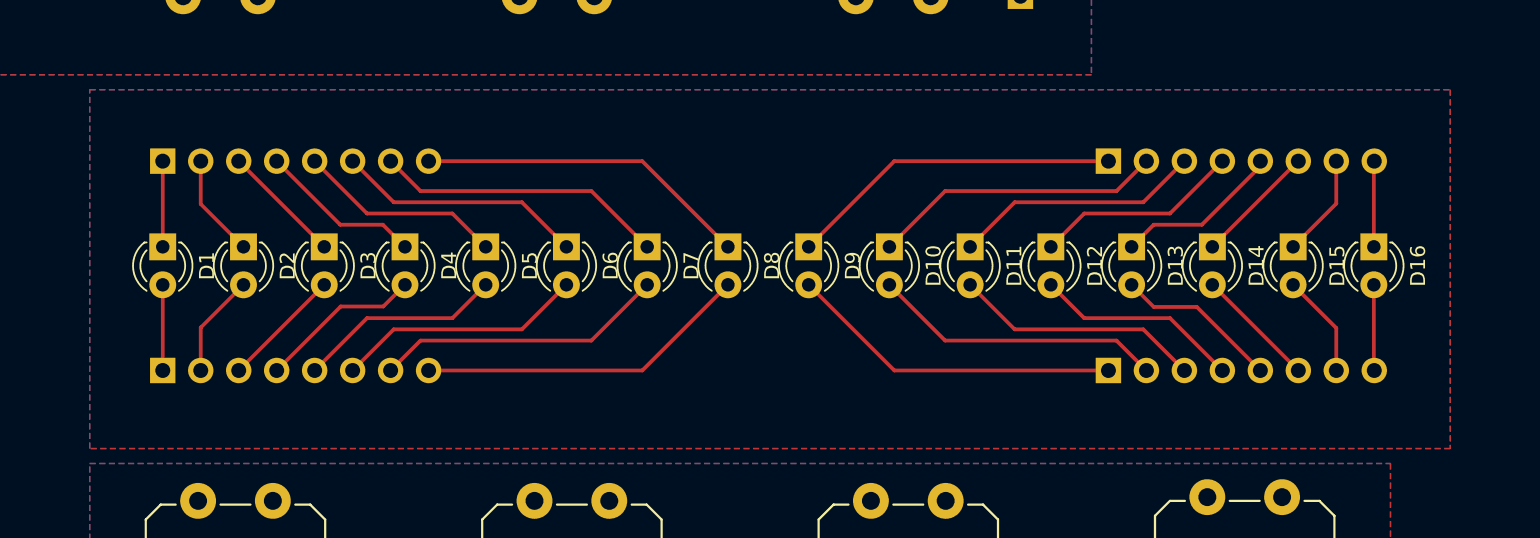
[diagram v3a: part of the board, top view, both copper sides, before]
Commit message: Add copper fill to LED board
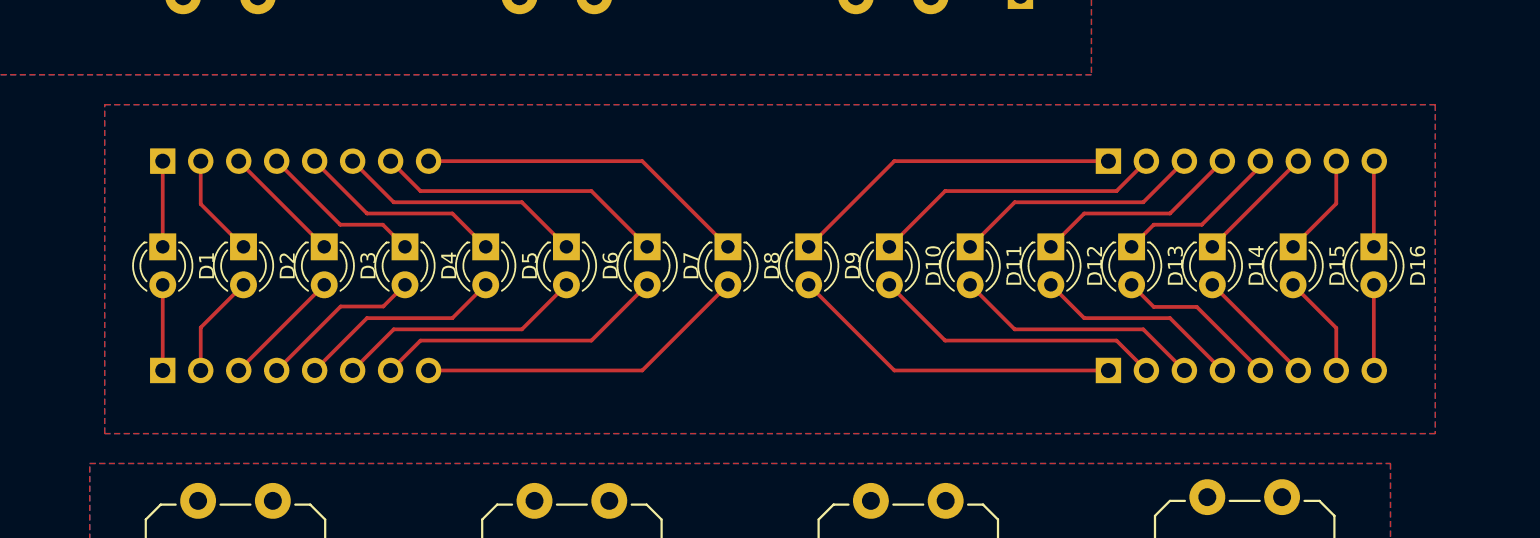
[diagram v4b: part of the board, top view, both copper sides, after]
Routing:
- added copper zone on B.Cu, net (none)
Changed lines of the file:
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@@
     (34 B.Paste user hide)
     (35 F.Paste user hide)
-    (36 B.SilkS user)
-    (37 F.SilkS user)
-    (38 B.Mask user)
-    (39 F.Mask user)
-    (40 Dwgs.User user)
+    (36 B.SilkS user hide)
+    (37 F.SilkS user hide)
+    (38 B.Mask user hide)
+    (39 F.Mask user hide)
+    (40 Dwgs.User user hide)
     (41 Cmts.User user hide)
     (42 Eco1.User user hide)
@@
     (44 Edge.Cuts user hide)
     (45 Margin user hide)
-    (46 B.CrtYd user)
-    (47 F.CrtYd user)
-    (48 B.Fab user)
-    (49 F.Fab user)
+    (46 B.CrtYd user hide)
+    (47 F.CrtYd user hide)
+    (48 B.Fab user hide)
+    (49 F.Fab user hide)
   )
   (setup
@@
     (polygon
       (pts
-        (xy 375 108) (xy 466 108) (xy 466 132) (xy 375 132)
+        (xy 258 84) (xy 442 84) (xy 442 107) (xy 258 107)
       )
     )
   )
-  (zone (net 0) (net_name "") (layer F.Cu) (hatch edge 0.508)
+  (zone (net 1) (net_name GND) (layer F.Cu) (hatch edge 0.508)
     (connect_pads (clearance 0.508))
     (min_thickness 0.254)
@@
     (polygon
       (pts
-        (xy 466 108) (xy 466 132) (xy 375 132) (xy 375 108)
+        (xy 258 84) (xy 442 84) (xy 442 107) (xy 258 107)
       )
     )
   )
-  (zone (net 1) (net_name GND) (layer B.Cu) (hatch edge 0.508)
+  (zone (net 0) (net_name "") (layer F.Cu) (hatch edge 0.508)
     (connect_pads (clearance 0.508))
     (min_thickness 0.254)
@@
     (polygon
       (pts
-        (xy 258 84) (xy 442 84) (xy 442 107) (xy 258 107)
+        (xy 376 109) (xy 465 109) (xy 465 131) (xy 376 131)
       )
     )
   )
-  (zone (net 1) (net_name GND) (layer F.Cu) (hatch edge 0.508)
+  (zone (net 0) (net_name "") (layer B.Cu) (hatch edge 0.508)
     (connect_pads (clearance 0.508))
     (min_thickness 0.254)
@@
     (polygon
       (pts
-        (xy 258 84) (xy 442 84) (xy 442 107) (xy 258 107)
+        (xy 376 109) (xy 465 109) (xy 465 131) (xy 376 131)
       )
     )

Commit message: Redesign of upper boards
Added bussed resistors following Igor's correction to the schematic + tidied schematic.
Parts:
- added RN4: 10k, Resistor_THT:R_Array_SIP9, F.Cu at (90.0, 141.5)
- added RN5: 10k, Resistor_THT:R_Array_SIP9, F.Cu at (135.0, 141.5)
- added RN6: 10k, Resistor_THT:R_Array_SIP9, F.Cu at (180.0, 141.5)
- added RN7: 10k, Resistor_THT:R_Array_SIP9, F.Cu at (224.9, 141.5)
- added RN8: 10k, Resistor_THT:R_Array_SIP9, F.Cu at (396.0, 141.5)
- added RN9: 10k, Resistor_THT:R_Array_SIP9, F.Cu at (441.0, 141.5)
- moved SW_F1 490.6 mm to (420.3, 278.0)
- moved H22 481.6 mm to (69.0, 326.0)
- moved RN1 469.7 mm to (443.1, 266.5), turned to 180 degrees
- moved H17 462.7 mm to (69.0, 258.0)
- moved H26 195.5 mm to (465.8, 326.0)
- moved PT_25 181.1 mm to (432.0, 243.0)
- moved PT_31 164.2 mm to (270.0, 270.0)
- moved H21 142.7 mm to (447.2, 243.0)
- moved PT_26 135.0 mm to (405.0, 243.0)
- moved D1 123.7 mm to (261.9, 82.8)
- moved D10 123.7 mm to (310.5, 82.8)
- moved D11 123.7 mm to (315.9, 82.8)
- moved D12 123.7 mm to (321.3, 82.8)
- moved D13 123.7 mm to (326.7, 82.8)
- moved D14 123.7 mm to (332.1, 82.8)
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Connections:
- SW1 pad 4: GND -> +5V
- SW10 pad 3: GND -> Net-(SW10-Pad3)
- SW10 pad 4: Net-(SW10-Pad4) -> +5V
- SW11 pad 3: GND -> +5V
- SW12 pad 3: GND -> +5V
- SW13 pad 3: GND -> +5V
- SW14 pad 3: GND -> +5V
- SW15 pad 3: GND -> +5V
- SW16 pad 3: GND -> +5V
- SW17 pad 3: GND -> Net-(SW17-Pad3)
- SW17 pad 4: Net-(SW17-Pad4) -> +5V
- SW18 pad 3: GND -> Net-(SW18-Pad3)
- SW18 pad 4: Net-(SW18-Pad4) -> +5V
- SW19 pad 3: GND -> Net-(SW19-Pad3)
- SW19 pad 4: Net-(SW19-Pad4) -> +5V
- SW2 pad 3: GND -> Net-(SW2-Pad3)
- SW2 pad 4: Net-(SW2-Pad4) -> +5V
- SW20 pad 3: GND -> Net-(SW20-Pad3)
- SW20 pad 4: Net-(SW20-Pad4) -> +5V
- SW21 pad 3: GND -> Net-(SW21-Pad3)
- SW21 pad 4: Net-(SW21-Pad4) -> +5V
- SW22 pad 3: GND -> Net-(SW22-Pad3)
- SW22 pad 4: Net-(SW22-Pad4) -> +5V
- SW23 pad 3: Net-(SW23-Pad3) -> +5V
- SW23 pad 4: GND -> Net-(SW23-Pad4)
- SW24 pad 4: GND -> +5V
- SW25 pad 3: GND -> +5V
- SW26 pad 3: GND -> Net-(SW26-Pad3)
- SW26 pad 4: Net-(SW26-Pad4) -> +5V
- SW27 pad 3: GND -> +5V
- SW28 pad 3: GND -> +5V
- SW29 pad 3: GND -> +5V
- SW3 pad 3: GND -> Net-(SW3-Pad3)
- SW3 pad 4: Net-(SW3-Pad4) -> +5V
- SW30 pad 3: GND -> +5V
- SW31 pad 3: GND -> +5V
- SW32 pad 3: GND -> +5V
- SW4 pad 3: GND -> Net-(SW4-Pad3)
- SW4 pad 4: Net-(SW4-Pad4) -> +5V
- SW41 pad 3: GND -> Net-(SW41-Pad3)
- SW41 pad 4: Net-(SW41-Pad4) -> +5V
- SW42 pad 3: GND -> Net-(SW42-Pad3)
- SW42 pad 4: Net-(SW42-Pad4) -> +5V
- SW43 pad 3: GND -> Net-(SW43-Pad3)
- SW43 pad 4: Net-(SW43-Pad4) -> +5V
- SW44 pad 3: GND -> Net-(SW44-Pad3)
- SW44 pad 4: Net-(SW44-Pad4) -> +5V
- SW45 pad 3: GND -> Net-(SW45-Pad3)
- SW45 pad 4: Net-(SW45-Pad4) -> +5V
- SW46 pad 3: GND -> Net-(SW46-Pad3)
- SW46 pad 4: Net-(SW46-Pad4) -> +5V
- SW47 pad 3: GND -> +5V
- SW48 pad 3: GND -> Net-(SW48-Pad3)
- SW48 pad 4: Net-(SW48-Pad4) -> +5V
- SW49 pad 3: GND -> +5V
- SW5 pad 3: GND -> Net-(SW5-Pad3)
- SW5 pad 4: Net-(SW5-Pad4) -> +5V
- SW50 pad 3: GND -> Net-(SW50-Pad3)
- SW50 pad 4: Net-(SW50-Pad4) -> +5V
- SW51 pad 3: GND -> +5V
- SW52 pad 3: GND -> +5V
- SW53 pad 3: GND -> +5V
- SW54 pad 3: GND -> +5V
- SW55 pad 3: GND -> +5V
- SW56 pad 3: GND -> +5V
- SW6 pad 3: GND -> Net-(SW6-Pad3)
- SW6 pad 4: Net-(SW6-Pad4) -> +5V
- SW7 pad 3: GND -> +5V
- SW8 pad 3: GND -> Net-(SW8-Pad3)
- SW8 pad 4: Net-(SW8-Pad4) -> +5V
- SW9 pad 3: GND -> +5V
- U6 pad 16: Net-(RVCF1-Pad2) -> Net-(PT_31-Pad2)
- U6 pad 17: Net-(PT_31-Pad2) -> Net-(PT_30-Pad2)
- U6 pad 18: Net-(PT_30-Pad2) -> Net-(PT_29-Pad2)
- U6 pad 19: Net-(PT_29-Pad2) -> Net-(PT_28-Pad2)
- U6 pad 20: Net-(PT_28-Pad2) -> Net-(PT_27-Pad2)
- U6 pad 21: Net-(PT_27-Pad2) -> Net-(PT_26-Pad2)
- U6 pad 22: Net-(PT_26-Pad2) -> Net-(PT_25-Pad2)
- U6 pad 23: Net-(PT_25-Pad2) -> Net-(RVCF1-Pad2)
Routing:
- net +5V: track 1074.5 -> 2497.5 mm, vias 3 -> 0
- net S2: track 217.0 -> 585.6 mm, vias 0 -> 1
- net S3: track 218.3 -> 585.8 mm, vias 0 -> 1
- net S1: track 218.3 -> 567.8 mm, vias 0 -> 1
- net S0: track 217.2 -> 566.7 mm, vias 0 -> 1
- net Net-(PT_25-Pad2): track 0.00 -> 137.7 mm
- net Net-(RV4-Pad2): track 0.00 -> 136.5 mm
- net /37: track 0.00 -> 134.8 mm
- net Net-(RVCF1-Pad2): track 0.00 -> 131.8 mm, vias 0 -> 1
- net /35: track 0.00 -> 127.7 mm
- net Net-(RV5-Pad2): track 0.00 -> 111.8 mm
- net Net-(PT_26-Pad2): track 0.00 -> 111.8 mm
- net Net-(PT_27-Pad2): track 0.00 -> 88.8 mm
- net Net-(RV3-Pad2): track 0.00 -> 86.9 mm
- net Net-(RV6-Pad2): track 0.00 -> 81.1 mm
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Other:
- board text added: "Alt Switch position"
- board text added: "Traces only inside Box"
